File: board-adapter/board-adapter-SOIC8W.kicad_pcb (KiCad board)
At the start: 2 copper layers, 6 x 6 mm, 9 parts, among them J101 Conn_01x01_Female, J102 Conn_01x01_Female, J103 Conn_01x01_Female, J104 Conn_02x04_Odd_Even, J105 Conn_01x01_Female, J106 Conn_01x01_Female, J107 Conn_01x01_Female, J108 Conn_01x01_Female, J109 Conn_01x01_Female

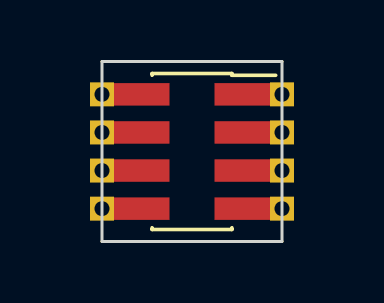
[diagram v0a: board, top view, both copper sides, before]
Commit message: fix SOIC8W adapter pin row pitch
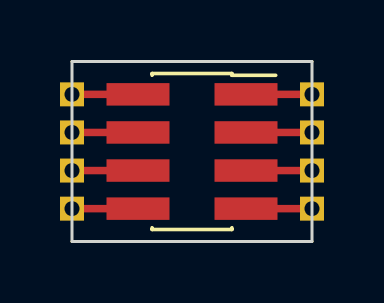
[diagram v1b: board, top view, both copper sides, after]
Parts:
- moved J101 1.00 mm to (96.0, 98.1)
- moved J102 1.00 mm to (104.0, 98.1)
- moved J103 1.00 mm to (96.0, 99.4)
- moved J105 1.00 mm to (104.0, 99.4)
- moved J106 1.00 mm to (96.0, 100.6)
- moved J107 1.00 mm to (104.0, 100.6)
- moved J108 1.00 mm to (96.0, 101.9)
- moved J109 1.00 mm to (104.0, 101.9)
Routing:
- net GND: track 1.20 -> 2.20 mm
- net /~CS: track 1.20 -> 2.20 mm
- net /VCC: track 1.20 -> 2.20 mm
- net /IO3_~HOLD: track 1.20 -> 2.20 mm
- net /IO2_~WP: track 1.20 -> 2.20 mm
- net /IO1_DO: track 1.20 -> 2.20 mm
- net /IO0_DI: track 1.20 -> 2.20 mm
- net /CLK: track 1.20 -> 2.20 mm
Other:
- board size 6 x 6 mm -> 8 x 6 mm
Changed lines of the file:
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@@
   )
   (module Connector_PinHeader_1.27mm:PinHeader_1x01_P1.27mm_Vertical (layer F.Cu)
-    (at 103 99.365)
+    (at 104 99.365)
     (descr "Through hole straight pin header, 1x01, 1.27mm pitch, single row")
     (tags "Through hole pin header THT 1x01 1.27mm single row")
@@
   )
   (module Connector_PinHeader_1.27mm:PinHeader_1x01_P1.27mm_Vertical (layer F.Cu)
-    (at 103 101.905)
+    (at 104 101.905)
     (descr "Through hole straight pin header, 1x01, 1.27mm pitch, single row")
     (tags "Through hole pin header THT 1x01 1.27mm single row")
@@
   )
   (module Connector_PinHeader_1.27mm:PinHeader_1x01_P1.27mm_Vertical (layer F.Cu)
-    (at 103 100.635)
+    (at 104 100.635)
     (descr "Through hole straight pin header, 1x01, 1.27mm pitch, single row")
     (tags "Through hole pin header THT 1x01 1.27mm single row")
@@
   )
   (module Connector_PinHeader_1.27mm:PinHeader_1x01_P1.27mm_Vertical (layer F.Cu)
-    (at 97 100.635)
+    (at 96 100.635)
     (descr "Through hole straight pin header, 1x01, 1.27mm pitch, single row")
     (tags "Through hole pin header THT 1x01 1.27mm single row")
@@
   )
   (module Connector_PinHeader_1.27mm:PinHeader_1x01_P1.27mm_Vertical (layer F.Cu)
-    (at 97 101.905)
+    (at 96 101.905)
     (descr "Through hole straight pin header, 1x01, 1.27mm pitch, single row")
     (tags "Through hole pin header THT 1x01 1.27mm single row")
@@
   )
   (module Connector_PinHeader_1.27mm:PinHeader_1x01_P1.27mm_Vertical (layer F.Cu)
-    (at 97 99.365)
+    (at 96 99.365)
     (descr "Through hole straight pin header, 1x01, 1.27mm pitch, single row")
     (tags "Through hole pin header THT 1x01 1.27mm single row")
@@
   )
   (module Connector_PinHeader_1.27mm:PinHeader_1x01_P1.27mm_Vertical (layer F.Cu)
-    (at 97 98.095)
+    (at 96 98.095)
     (descr "Through hole straight pin header, 1x01, 1.27mm pitch, single row")
     (tags "Through hole pin header THT 1x01 1.27mm single row")
@@
   )
   (module Connector_PinHeader_1.27mm:PinHeader_1x01_P1.27mm_Vertical (layer F.Cu)
-    (at 103 98.095)
+    (at 104 98.095)
     (descr "Through hole straight pin header, 1x01, 1.27mm pitch, single row")
     (tags "Through hole pin header THT 1x01 1.27mm single row")
@@
     )
   )
-  (gr_line (start 97 103) (end 97 97) (layer Edge.Cuts) (width 0.1))
-  (gr_line (start 103 103) (end 97 103) (layer Edge.Cuts) (width 0.1))
-  (gr_line (start 103 97) (end 103 103) (layer Edge.Cuts) (width 0.1))
-  (gr_line (start 97 97) (end 103 97) (layer Edge.Cuts) (width 0.1))
-  (segment (start 97 101.905) (end 98.2 101.905) (width 0.25) (layer F.Cu) (net 1))
-  (segment (start 97 98.095) (end 98.2 98.095) (width 0.25) (layer F.Cu) (net 2))
-  (segment (start 101.8 98.095) (end 103 98.095) (width 0.25) (layer F.Cu) (net 3))
-  (segment (start 97 99.365) (end 98.2 99.365) (width 0.25) (layer F.Cu) (net 4))
-  (segment (start 101.8 99.365) (end 103 99.365) (width 0.25) (layer F.Cu) (net 5))
-  (segment (start 103 100.635) (end 101.8 100.635) (width 0.25) (layer F.Cu) (net 6))
-  (segment (start 98.2 100.635) (end 97 100.635) (width 0.25) (layer F.Cu) (net 7))
-  (segment (start 103 101.905) (end 101.8 101.905) (width 0.25) (layer F.Cu) (net 8))
+  (gr_line (start 96 103) (end 96 97) (layer Edge.Cuts) (width 0.1))
+  (gr_line (start 104 103) (end 96 103) (layer Edge.Cuts) (width 0.1))
+  (gr_line (start 104 97) (end 104 103) (layer Edge.Cuts) (width 0.1))
+  (gr_line (start 96 97) (end 104 97) (layer Edge.Cuts) (width 0.1))
+  (segment (start 96 101.905) (end 98.2 101.905) (width 0.25) (layer F.Cu) (net 1))
+  (segment (start 96 98.095) (end 98.2 98.095) (width 0.25) (layer F.Cu) (net 2))
+  (segment (start 101.8 98.095) (end 104 98.095) (width 0.25) (layer F.Cu) (net 3))
+  (segment (start 96 99.365) (end 98.2 99.365) (width 0.25) (layer F.Cu) (net 4))
+  (segment (start 104 99.365) (end 101.8 99.365) (width 0.25) (layer F.Cu) (net 5))
+  (segment (start 101.8 100.635) (end 104 100.635) (width 0.25) (layer F.Cu) (net 6))
+  (segment (start 96 100.635) (end 98.2 100.635) (width 0.25) (layer F.Cu) (net 7))
+  (segment (start 104 101.905) (end 101.8 101.905) (width 0.25) (layer F.Cu) (net 8))
 )

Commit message: increase trace width
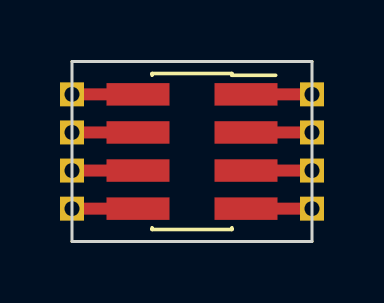
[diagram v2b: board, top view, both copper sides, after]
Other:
- net class Default: trace_width 0.25 -> 0.4; via_dia 0.8 -> 0.6; via_drill 0.4 -> 0.3
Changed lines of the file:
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@@
   )
   (setup
-    (last_trace_width 0.25)
+    (last_trace_width 0.4)
     (trace_clearance 0.2)
     (zone_clearance 0.508)
@@
     (segment_width 0.2)
     (edge_width 0.1)
-    (via_size 0.8)
-    (via_drill 0.4)
+    (via_size 0.6)
+    (via_drill 0.3)
     (via_min_size 0.4)
     (via_min_drill 0.3)
@@
   (net_class Default "This is the default net class."
     (clearance 0.2)
-    (trace_width 0.25)
-    (via_dia 0.8)
-    (via_drill 0.4)
+    (trace_width 0.4)
+    (via_dia 0.6)
+    (via_drill 0.3)
     (uvia_dia 0.3)
     (uvia_drill 0.1)
@@
   (gr_line (start 104 97) (end 104 103) (layer Edge.Cuts) (width 0.1))
   (gr_line (start 96 97) (end 104 97) (layer Edge.Cuts) (width 0.1))
-  (segment (start 96 101.905) (end 98.2 101.905) (width 0.25) (layer F.Cu) (net 1))
-  (segment (start 96 98.095) (end 98.2 98.095) (width 0.25) (layer F.Cu) (net 2))
-  (segment (start 101.8 98.095) (end 104 98.095) (width 0.25) (layer F.Cu) (net 3))
-  (segment (start 96 99.365) (end 98.2 99.365) (width 0.25) (layer F.Cu) (net 4))
-  (segment (start 104 99.365) (end 101.8 99.365) (width 0.25) (layer F.Cu) (net 5))
-  (segment (start 101.8 100.635) (end 104 100.635) (width 0.25) (layer F.Cu) (net 6))
-  (segment (start 96 100.635) (end 98.2 100.635) (width 0.25) (layer F.Cu) (net 7))
-  (segment (start 104 101.905) (end 101.8 101.905) (width 0.25) (layer F.Cu) (net 8))
+  (segment (start 96 101.905) (end 98.2 101.905) (width 0.4) (layer F.Cu) (net 1))
+  (segment (start 96 98.095) (end 98.2 98.095) (width 0.4) (layer F.Cu) (net 2))
+  (segment (start 101.8 98.095) (end 104 98.095) (width 0.4) (layer F.Cu) (net 3))
+  (segment (start 96 99.365) (end 98.2 99.365) (width 0.4) (layer F.Cu) (net 4))
+  (segment (start 104 99.365) (end 101.8 99.365) (width 0.4) (layer F.Cu) (net 5))
+  (segment (start 101.8 100.635) (end 104 100.635) (width 0.4) (layer F.Cu) (net 6))
+  (segment (start 96 100.635) (end 98.2 100.635) (width 0.4) (layer F.Cu) (net 7))
+  (segment (start 104 101.905) (end 101.8 101.905) (width 0.4) (layer F.Cu) (net 8))
 )

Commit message: remove pin 1 markers from wrong position
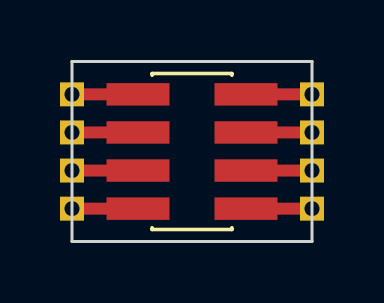
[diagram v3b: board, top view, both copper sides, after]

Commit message: update pad to mask clearance
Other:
- rule pad_to_mask_clearance: 0.2 -> 0.1
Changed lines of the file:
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@@
     (pad_size 0.8 0.8)
     (pad_drill 0.5)
-    (pad_to_mask_clearance 0.2)
+    (pad_to_mask_clearance 0.1)
     (aux_axis_origin 0 0)
     (visible_elements FFFFFF7F)
